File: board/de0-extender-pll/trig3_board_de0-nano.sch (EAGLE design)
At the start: 305 parts, among them IC1 ICL7660CPA, IC2 ICL7660CPA, IC3 ICL7660CPA, IC4 ICL7660CPA, J10 2p-2.54, J11 2p-2.54, J12 4p-2.54, J13 BU-SMB-V, J131 4p-2.54, J14 BU-SMB-V, J141 2p-2.54, J15 2p-2.54, J16 2p-2.54, J17 2p-2.54, J18 2p-2.54, J19 6HE-160-VG64AC, J20 4p-2.54, J21 4p-2.54, J22 2p-2.54, J23 2p-2.54, J24 2p-2.54, J25 2p-2.54, J26 4p-2.54, J27 4p-2.54, J28 2p-2.54, J29 2p-2.54, J3 4p-2.54, J30 2p-2.54, J31 2p-2.54, J311 4p-2.54, J32 2p-2.54, J33 2p-2.54, J34 2p-2.54, J35 2p-2.54, J36 2p-2.54, J37 2p-2.54, J38 2p-2.54, J39 2p-2.54, J4 2p-2.54, J40 2p-2.54, J41 2p-2.54, J42 2p-2.54, J43 2p-2.54, J48 2p-2.54, J49 2p-2.54, J5 2p-2.54, J50 2p-2.54, J51 2p-2.54, J52 2p-2.54, J53 2p-2.54, J54 2p-2.54, J55 2p-2.54, J6 2p-2.54, J7 4p-2.54, J8 2p-2.54, J9 2p-2.54, K15_R10P BU-SMB-V, K16_R10N BU-SMB-V, M16CLK_3N BU-SMB-V, P11 BU-SMB-V, P14_CLKOUT_4P BU-SMB-V, P15 BU-SMB-V, P16_R15N BU-SMB-V, P9 BU-SMB-V, T10_B16N BU-SMB-V, T12_B18N BU-SMB-V, T13_B20N BU-SMB-V, T14_B23P BU-SMB-V, T15_B23N BU-SMB-V, T9CLK_7N BU-SMB-V

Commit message: removed some unused inputs
kept all clock inputs and some extra inputs
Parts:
- removed A14_CLKOUT_2N, B7_T9P, C3_CLKOUT_3N, C9_T15N, D3_CLKOUT_3P, D9_T15P, G15_R5P, G16_R5N, N15_R13P, N16_R13N, P14_CLKOUT_4P, R10_B16P, R12_B18P, R14_CLKOUT_4N, T10_B16N, T12_B18N: BU-SMB-V, con-coax:BU-SMB-V
- removed J10, J11, J28, J29, J30, J31, J48, J49, J50, J51, J52, J53, J54, J55, J8, J9: 2p-2.54, Seeed-Connector:DIP-BLACK-MALE-HEADER-VERT(2P-2.54)
- removed R100, R111, R141, R24, R26, R27, R29, R45, R46, R47, R49, R50, R51, R52, R53, R91: 50, SparkFun-Passives:RESISTORAXIAL-0.3
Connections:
- net GND: no longer A14_CLKOUT_2N.2, B7_T9P.2, C3_CLKOUT_3N.2, C9_T15N.2, D3_CLKOUT_3P.2, D9_T15P.2, G15_R5P.2, G16_R5N.2, J10.1, J11.1, J28.1, J29.1, J30.1, J31.1, J48.1, J49.1, J50.1, J51.1, J52.1, J53.1, J54.1, J55.1, J8.1, J9.1, N15_R13P.2, N16_R13N.2, P14_CLKOUT_4P.2, R100.1, R10_B16P.2, R111.1, R12_B18P.2, R141.1, R14_CLKOUT_4N.2, R24.1, R26.1, R27.1, R29.1, R45.1, R46.1, R47.1, R49.1, R50.1, R51.1, R52.1, R53.1, R91.1, T10_B16N.2, T12_B18N.2
- net GPIO_00_D3: no longer D3_CLKOUT_3P.1, J50.2, R51.2
- net GPIO_012_B7: no longer B7_T9P.1, J49.2, R50.2
- net GPIO_01_C3: no longer C3_CLKOUT_3N.1, J30.2, R27.2
- net GPIO_024_C9: no longer C9_T15N.1, J8.2, R91.2
- net GPIO_025_D9: no longer D9_T15P.1, J11.2, R141.2
- net GPIO_111_R10: no longer J48.2, R10_B16P.1, R49.2
- net GPIO_122_R14: no longer J53.2, R14_CLKOUT_4N.1, R46.2
- net GPIO_123_N16: no longer J55.2, N16_R13N.1, R52.2
- net GPIO_124_N15: no longer J54.2, N15_R13P.1, R47.2
- net GPIO_125_P14: no longer J52.2, P14_CLKOUT_4P.1, R45.2
- net GPIO_15_T12: no longer J9.2, R100.2, T12_B18N.1
- net GPIO_16_R12: no longer J10.2, R111.2, R12_B18P.1
- net GPIO_18_T10: no longer J51.2, R53.2, T10_B16N.1
- net GPIO_20_A14: no longer A14_CLKOUT_2N.1, J31.2, R29.2
- net GPIO_211_G16: no longer G16_R5N.1, J28.2, R24.2
- net GPIO_212_G15: no longer G15_R5P.1, J29.2, R26.2
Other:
- note added: "pins used in design A6 B6 C11 E11 F9 K15 K16 L13 L14 N9 N11 P16 R9 R16 T9 R9/T9 N9 L13 L14 R16/P16 B6 A6 K15/K16 N11 F9 C11 E11 on board: clock R8, LEDs L3 B1 F3 D1 A11 B13 A13 A15 IN: K15, K16, P16 R16 R9 T9 OUT: A6, B6, C11, E11, N9, N11, F9 SERIAL: L13, L14"
- moved on the sheet: A12_T21N, A2_T2N, A3_T2P, A8CLK_4N, B12_T21P, B8CLK_4P, E15CLK_2P, E16CLK_2N, F8_T10P, K15_R10P, M16CLK_3N, R11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

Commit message: removed many outputs and negative voltage
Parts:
- removed A4, A5, B11, B16, B3, B4, B5, C14, C15, C6, C8, D11, D12, D14, D15, D16, D5, D6, D8, E10, E6, E9, F14, F15, F16, J14, N12, N14: BU-SMB-V, con-coax:BU-SMB-V
- removed C10, C5, C91, C93, C94, C95, C97: 0.1uF, SparkFun-Capacitors:CAP0805
- removed OJ1, OJ17, OJ18, OJ19, OJ2, OJ20, OJ21, OJ22, OJ23, OJ24, OJ25, OJ26, OJ27, OJ28, OJ29, OJ3, OJ30, OJ31, OJ32, OJ33, OJ34, OJ35, OJ36, OJ37, OJ38, OJ39, OJ4, OJ40, OJ49, OJ5, OJ50, OJ51, OJ52, OJ53, OJ54, OJ55, OJ56, OJ6, OJ65, OJ66, OJ67, OJ68, OJ69, OJ7, OJ70, OJ71, OJ72, OJ8, OJ89, OJ90, OJ91, OJ92, OJ93, OJ94, OJ95, OJ96: 2p-2.54, Seeed-Connector:DIP-BLACK-MALE-HEADER-VERT(2P-2.54)
- removed VSLUE, VSLUE11, VSLUE2, VSLUE3, VSLUE4, VSLUE6, VSLUE8: SN74ACT244DW, SN74ACT244DW:SN74ACT244DW
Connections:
- removed net OUT1: J14.1, OJ1.1, VSLUE.1Y1, VSLUE.1Y2
- removed net OUT10: E9.1, OJ19.1, VSLUE2.1Y3, VSLUE2.1Y4
- removed net OUT11: D8.1, OJ17.1, VSLUE2.2Y3, VSLUE2.2Y4
- removed net OUT12: B16.1, OJ18.1, VSLUE2.2Y1, VSLUE2.2Y2
- removed net OUT13: C15.1, OJ28.1, VSLUE3.1Y1, VSLUE3.1Y2
- removed net OUT14: C14.1, OJ27.1, VSLUE3.1Y3, VSLUE3.1Y4
- removed net OUT15: D15.1, OJ25.1, VSLUE3.2Y3, VSLUE3.2Y4
- removed net OUT16: F14.1, OJ26.1, VSLUE3.2Y1, VSLUE3.2Y2
- removed net OUT17: D16.1, OJ36.1, VSLUE4.1Y1, VSLUE4.1Y2
- removed net OUT18: D14.1, OJ35.1, VSLUE4.1Y3, VSLUE4.1Y4
- removed net OUT19: F15.1, OJ33.1, VSLUE4.2Y3, VSLUE4.2Y4
- removed net OUT2: D11.1, OJ2.1, VSLUE.1Y3, VSLUE.1Y4
- removed net OUT20: F16.1, OJ34.1, VSLUE4.2Y1, VSLUE4.2Y2
- removed net OUT25: D6.1, OJ52.1, VSLUE6.1Y1, VSLUE6.1Y2
- removed net OUT26: C6.1, OJ51.1, VSLUE6.1Y3, VSLUE6.1Y4
- removed net OUT27: C8.1, OJ49.1, VSLUE6.2Y3, VSLUE6.2Y4
- removed net OUT28: E6.1, OJ50.1, VSLUE6.2Y1, VSLUE6.2Y2
- removed net OUT3: B11.1, OJ3.1, VSLUE.2Y1, VSLUE.2Y2
- removed net OUT33: B5.1, OJ68.1, VSLUE8.1Y1, VSLUE8.1Y2
- removed net OUT34: A5.1, OJ67.1, VSLUE8.1Y3, VSLUE8.1Y4
- removed net OUT35: D5.1, OJ65.1, VSLUE8.2Y3, VSLUE8.2Y4
- removed net OUT36: N14.1, OJ66.1, VSLUE8.2Y1, VSLUE8.2Y2
- removed net OUT4: E10.1, OJ4.1, VSLUE.2Y3, VSLUE.2Y4
- removed net OUT45: D12.1, OJ92.1, VSLUE11.1Y1, VSLUE11.1Y2
- removed net OUT46: B3.1, OJ91.1, VSLUE11.1Y3, VSLUE11.1Y4
- removed net OUT47: A4.1, OJ89.1, VSLUE11.2Y3, VSLUE11.2Y4
- removed net OUT48: B4.1, OJ90.1, VSLUE11.2Y1, VSLUE11.2Y2
- removed net OUT9: N12.1, OJ20.1, VSLUE2.1Y1, VSLUE2.1Y2
- net 5V: no longer C10.2, C5.2, C91.2, C93.2, C94.2, C95.2, C97.2, VSLUE.VCC, VSLUE11.VCC, VSLUE2.VCC, VSLUE3.VCC, VSLUE4.VCC, VSLUE6.VCC, VSLUE8.VCC
- net GND: no longer A4.2, A5.2, B11.2, B16.2, B3.2, B4.2, B5.2, C10.1, C14.2, C15.2, C5.1, C6.2, C8.2, C91.1, C93.1, C94.1, C95.1, C97.1, D11.2, D12.2, D14.2, D15.2, D16.2, D5.2, D6.2, D8.2, E10.2, E6.2, E9.2, F14.2, F15.2, F16.2, J14.2, N12.2, N14.2, OJ1.2, OJ17.2, OJ18.2, OJ19.2, OJ2.2, OJ20.2, OJ21.2, OJ22.2, OJ23.2, OJ24.2, OJ25.2, OJ26.2, OJ27.2, OJ28.2, OJ29.2, OJ3.2, OJ30.2, OJ31.2, OJ32.2, OJ33.2, OJ34.2, OJ35.2, OJ36.2, OJ37.2, OJ38.2, OJ39.2, OJ4.2, OJ40.2, OJ49.2, OJ5.2, OJ50.2, OJ51.2, OJ52.2, OJ53.2, OJ54.2, OJ55.2, OJ56.2, OJ6.2, OJ65.2, OJ66.2, OJ67.2, OJ68.2, OJ69.2, OJ7.2, OJ70.2, OJ71.2, OJ72.2, OJ8.2, OJ89.2, OJ90.2, OJ91.2, OJ92.2, OJ93.2, OJ94.2, OJ95.2, OJ96.2, VSLUE.GND, VSLUE11.GND, VSLUE2.GND, VSLUE3.GND, VSLUE4.GND, VSLUE6.GND, VSLUE8.GND
- net GPIO_013_D6: no longer OJ55.1, VSLUE6.1A1, VSLUE6.1A2
- net GPIO_015_C6: no longer OJ56.1, VSLUE6.1A3, VSLUE6.1A4
- net GPIO_016_C8: no longer OJ53.1, VSLUE6.2A3, VSLUE6.2A4
- net GPIO_017_E6: no longer OJ54.1, VSLUE6.2A1, VSLUE6.2A2
- net GPIO_019_D8: no longer OJ21.1, VSLUE2.2A3, VSLUE2.2A4
- net GPIO_023_E9: no longer OJ24.1, VSLUE2.1A3, VSLUE2.1A4
- net GPIO_027_E10: no longer OJ5.1, VSLUE.2A3, VSLUE.2A4
- net GPIO_029_B11: no longer OJ6.1, VSLUE.2A1, VSLUE.2A2
- net GPIO_031_D11: no longer OJ8.1, VSLUE.1A3, VSLUE.1A4
- net GPIO_032_D12: no longer OJ95.1, VSLUE11.1A1, VSLUE11.1A2
- net GPIO_04_B3: no longer OJ96.1, VSLUE11.1A3, VSLUE11.1A4
- net GPIO_05_B4: no longer OJ94.1, VSLUE11.2A1, VSLUE11.2A2
- net GPIO_06_A4: no longer OJ93.1, VSLUE11.2A3, VSLUE11.2A4
- net GPIO_07_B5: no longer OJ71.1, VSLUE8.1A1, VSLUE8.1A2
- net GPIO_08_A5: no longer OJ72.1, VSLUE8.1A3, VSLUE8.1A4
- net GPIO_09_D5: no longer OJ69.1, VSLUE8.2A3, VSLUE8.2A4
- net GPIO_112_N12: no longer OJ23.1, VSLUE2.1A1, VSLUE2.1A2
- net GPIO_114_N9: no longer VSLUE.!1OE, VSLUE.!2OE, VSLUE11.!1OE, VSLUE11.!2OE, VSLUE2.!1OE, VSLUE2.!2OE, VSLUE3.!1OE, VSLUE3.!2OE, VSLUE4.!1OE, VSLUE4.!2OE, VSLUE6.!1OE, VSLUE6.!2OE, VSLUE8.!1OE, VSLUE8.!2OE
- net GPIO_127_N14: no longer OJ70.1, VSLUE8.2A1, VSLUE8.2A2
- net GPIO_133_J14: no longer OJ7.1, VSLUE.1A1, VSLUE.1A2
- net GPIO_210_F14: no longer OJ30.1, VSLUE3.2A1, VSLUE3.2A2
- net GPIO_21_B16: no longer OJ22.1, VSLUE2.2A1, VSLUE2.2A2
- net GPIO_22_C14: no longer OJ32.1, VSLUE3.1A3, VSLUE3.1A4
- net GPIO_24_C15: no longer OJ31.1, VSLUE3.1A1, VSLUE3.1A2
- net GPIO_25_D16: no longer OJ39.1, VSLUE4.1A1, VSLUE4.1A2
- net GPIO_26_D15: no longer OJ29.1, VSLUE3.2A3, VSLUE3.2A4
- net GPIO_27_D14: no longer OJ40.1, VSLUE4.1A3, VSLUE4.1A4
- net GPIO_28_F15: no longer OJ37.1, VSLUE4.2A3, VSLUE4.2A4
- net GPIO_29_F16: no longer OJ38.1, VSLUE4.2A1, VSLUE4.2A2

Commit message: more removal
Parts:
- removed C1, C12, C13, C17, C18, C3, C7, C9: 10uF, SparkFun-Capacitors:CAPPTH1
- removed C19, C20, C21, C22: 0.1uF, SparkFun-Capacitors:CAP0805
- removed IC1, IC2, IC3, IC4: ICL7660CPA, maxim:ICL7660CPA
- removed J1: (no value), SparkFun-Connectors:M13X22X13
- removed J131, J311: 4p-2.54, Seeed-Connector:DIP-BLACK-FEMALE-HEADER-VERT(4P-2.54)
- removed J19: 6HE-160-VG64AC, 19inch:6HE-160-VG64AC
- removed J20, J21, J26, J27: 4p-2.54, Seeed-Connector:DIP-BLACK-MALE-HEADER-VERT(4P-2.54)
- removed OJ10, OJ11, OJ12, OJ9: 2p-2.54, Seeed-Connector:DIP-BLACK-MALE-HEADER-VERT(2P-2.54)
- removed R1, R2, R3, R7: 3296W 5k, resistor:R-TRIMM3296W
- removed R10, R12, R13, R14: 1k, SparkFun-Passives:RESISTORAXIAL-0.3
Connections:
- removed net -3V3_1: C3.1, IC1.VOUT, J20.P$1, R10.2
- removed net -3V3_2: C9.1, IC2.VOUT, J21.P$1, R12.2
- removed net -3V3_3: C13.1, IC3.VOUT, J26.P$1, R13.2
- removed net -3V3_4: C18.1, IC4.VOUT, J27.P$1, R14.2
- removed net -V1: C19.2, J20.P$2, OJ9.1, R1.S
- removed net -V2: C20.2, J21.P$2, OJ10.1, R2.S
- removed net -V3: C21.2, J26.P$2, OJ11.1, R3.S
- removed net -V4: C22.2, J27.P$2, OJ12.1, R7.S
- removed net AIN0: J1.24, J131.P$4
- removed net AIN1: J1.25, J311.P$1
- removed net AIN2: J1.22, J131.P$3
- removed net AIN3: J1.21, J311.P$3
- removed net AIN4: J1.23, J311.P$2
- removed net AIN5: J1.18, J131.P$1
- removed net AIN6: J1.19, J311.P$4
- removed net AIN7: J1.20, J131.P$2
- removed net GPIO_20_A14: J1.5
- removed net GPIO_210_F14: J1.15
- removed net GPIO_211_G16: J1.16
- removed net GPIO_212_G15: J1.17
- removed net GPIO_21_B16: J1.6
- removed net GPIO_22_C14: J1.7
- removed net GPIO_24_C15: J1.9
- removed net GPIO_25_D16: J1.10
- removed net GPIO_26_D15: J1.11
- removed net GPIO_27_D14: J1.12
- removed net GPIO_28_F15: J1.13
- removed net GPIO_29_F16: J1.14
- removed net N$1: C1.1, IC1.CAP+
- removed net N$10: R1.E, R10.1
- removed net N$11: R12.1, R2.E
- removed net N$12: R13.1, R3.E
- removed net N$13: R14.1, R7.E
- removed net N$2: C1.2, IC1.CAP-
- removed net N$3: C12.1, IC3.CAP+
- removed net N$4: C7.1, IC2.CAP+
- removed net N$5: C7.2, IC2.CAP-
- removed net N$6: C12.2, IC3.CAP-
- removed net N$7: C17.1, IC4.CAP+
- removed net N$8: C17.2, IC4.CAP-
- net 3V3: no longer IC1.V+, IC2.V+, IC3.V+, IC4.V+, J1.1, J20.P$4, J21.P$4, J26.P$4, J27.P$4
- net 5V: no longer J191-A32.MS, J191-C32.MS, J192-A32.MS, J192-C32.MS
- net GND: no longer C13.2, C18.2, C19.1, C20.1, C21.1, C22.1, C3.2, C9.2, IC1.GND, IC2.GND, IC3.GND, IC4.GND, J1.26, J191-A9.MS, J191-C9.MS, J192-A9.MS, J192-C9.MS, J20.P$3, J21.P$3, J26.P$3, J27.P$3, R1.A, R2.A, R3.A, R7.A
- net GPIO_014_A7: no longer OJ9.2
- net GPIO_020_E8: no longer OJ12.2
- net GPIO_030_A12: no longer OJ10.2
- net GPIO_11_T15: no longer OJ11.2
- net GPIO_23_C16: no longer J1.8
- net GPIO_2_IN0_E15CLK: no longer J1.2
- net GPIO_2_IN1_E16CLK: no longer J1.3
- net GPIO_2_IN2_M16CLK: no longer J1.4

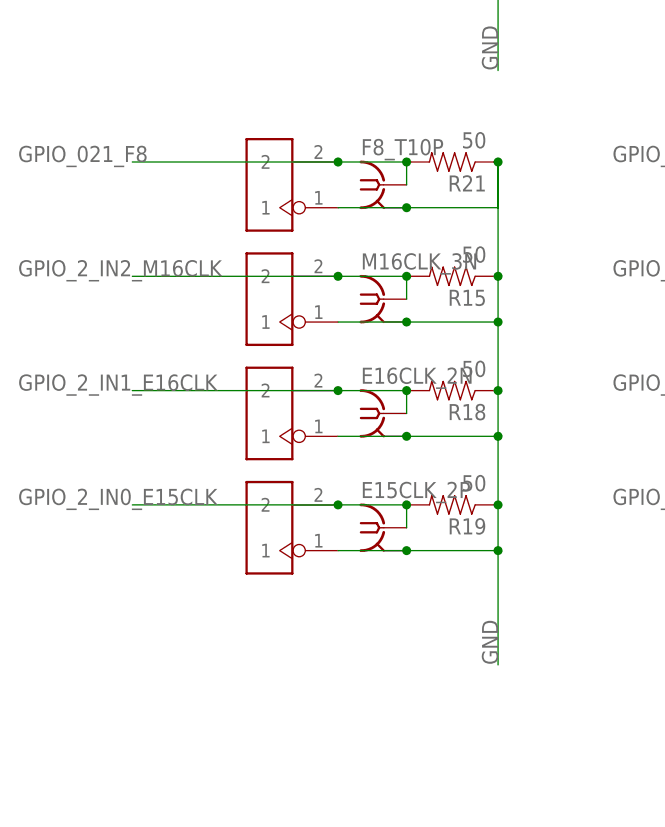
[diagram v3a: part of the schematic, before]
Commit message: going to delete more ins/outs
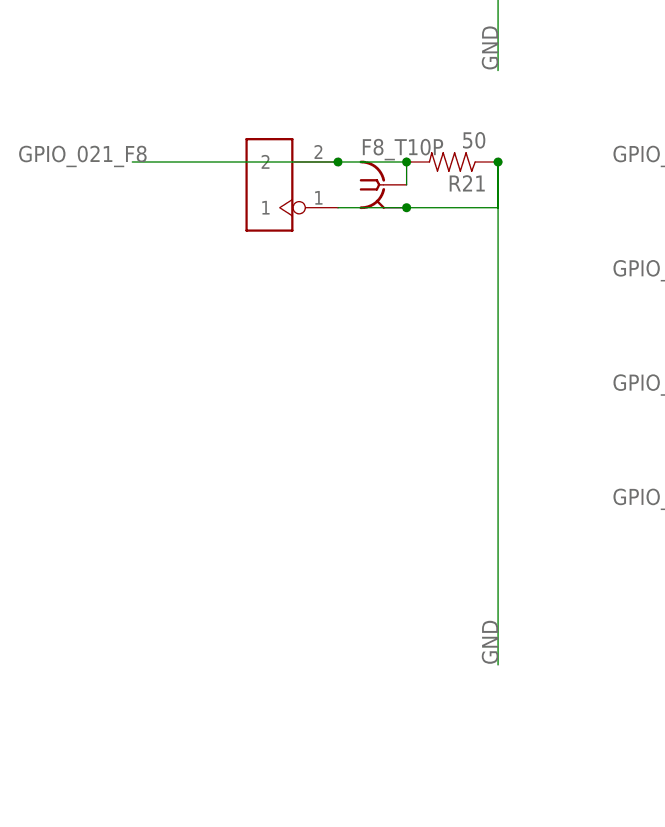
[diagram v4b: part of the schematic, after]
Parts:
- removed E15CLK_2P, E16CLK_2N, M16CLK_3N: BU-SMB-V, con-coax:BU-SMB-V
- removed J141, J15, J16: 2p-2.54, Seeed-Connector:DIP-BLACK-MALE-HEADER-VERT(2P-2.54)
- removed R15, R18, R19: 50, SparkFun-Passives:RESISTORAXIAL-0.3
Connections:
- removed net GPIO_2_IN0_E15CLK: E15CLK_2P.1, J16.2, R19.2
- removed net GPIO_2_IN1_E16CLK: E16CLK_2N.1, J15.2, R18.2
- removed net GPIO_2_IN2_M16CLK: J141.2, M16CLK_3N.1, R15.2
- net GND: no longer E15CLK_2P.2, E16CLK_2N.2, J141.1, J15.1, J16.1, M16CLK_3N.2, R15.1, R18.1, R19.1
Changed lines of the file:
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@@
 <part name="SV2" library="con-lsta" deviceset="FE20-2" device=""/>
 <part name="J2" library="SparkFun-Connectors" deviceset="M13X2" device="2X13"/>
-<part name="M16CLK_3N" library="con-coax" library_urn="urn:adsk.eagle:library:133" deviceset="BU-SMB-V" device="" package3d_urn="urn:adsk.eagle:package:6209/1"/>
-<part name="E16CLK_2N" library="con-coax" library_urn="urn:adsk.eagle:library:133" deviceset="BU-SMB-V" device="" package3d_urn="urn:adsk.eagle:package:6209/1"/>
-<part name="E15CLK_2P" library="con-coax" library_urn="urn:adsk.eagle:library:133" deviceset="BU-SMB-V" device="" package3d_urn="urn:adsk.eagle:package:6209/1"/>
-<part name="J141" library="Seeed-Connector" library_urn="urn:adsk.eagle:library:478" deviceset="DIP-BLACK-MALE-HEADER-VERT(2P-2.54)" device="" package3d_urn="urn:adsk.eagle:package:33132/1" value="2p-2.54"/>
-<part name="J15" library="Seeed-Connector" library_urn="urn:adsk.eagle:library:478" deviceset="DIP-BLACK-MALE-HEADER-VERT(2P-2.54)" device="" package3d_urn="urn:adsk.eagle:package:33132/1" value="2p-2.54"/>
-<part name="J16" library="Seeed-Connector" library_urn="urn:adsk.eagle:library:478" deviceset="DIP-BLACK-MALE-HEADER-VERT(2P-2.54)" device="" package3d_urn="urn:adsk.eagle:package:33132/1" value="2p-2.54"/>
-<part name="R15" library="SparkFun-Passives" deviceset="RESISTOR" device="AXIAL-0.3" value="50"/>
-<part name="R18" library="SparkFun-Passives" deviceset="RESISTOR" device="AXIAL-0.3" value="50"/>
-<part name="R19" library="SparkFun-Passives" deviceset="RESISTOR" device="AXIAL-0.3" value="50"/>
 <part name="F8_T10P" library="con-coax" library_urn="urn:adsk.eagle:library:133" deviceset="BU-SMB-V" device="" package3d_urn="urn:adsk.eagle:package:6209/1"/>
 <part name="J18" library="Seeed-Connector" library_urn="urn:adsk.eagle:library:478" deviceset="DIP-BLACK-MALE-HEADER-VERT(2P-2.54)" device="" package3d_urn="urn:adsk.eagle:package:33132/1" value="2p-2.54"/>
@@
 <attribute name="NAME" x="107.442" y="33.02" size="1.778" layer="95" rot="R270"/>
 </instance>
-<instance part="M16CLK_3N" gate="G1" x="-66.04" y="101.6" smashed="yes">
-<attribute name="NAME" x="-68.58" y="104.902" size="1.778" layer="95"/>
-</instance>
-<instance part="E16CLK_2N" gate="G1" x="-66.04" y="88.9" smashed="yes">
-<attribute name="NAME" x="-68.58" y="92.202" size="1.778" layer="95"/>
-</instance>
-<instance part="E15CLK_2P" gate="G1" x="-66.04" y="76.2" smashed="yes">
-<attribute name="NAME" x="-68.58" y="79.502" size="1.778" layer="95"/>
-</instance>
-<instance part="J141" gate="G$1" x="-78.74" y="101.6" smashed="yes" rot="R180"/>
-<instance part="J15" gate="G$1" x="-78.74" y="88.9" smashed="yes" rot="R180"/>
-<instance part="J16" gate="G$1" x="-78.74" y="76.2" smashed="yes" rot="R180"/>
-<instance part="R15" gate="G$1" x="-58.42" y="104.14" smashed="yes" rot="R180">
-<attribute name="NAME" x="-54.61" y="102.6414" size="1.778" layer="95" rot="R180"/>
-<attribute name="VALUE" x="-54.61" y="107.442" size="1.778" layer="96" rot="R180"/>
-</instance>
-<instance part="R18" gate="G$1" x="-58.42" y="91.44" smashed="yes" rot="R180">
-<attribute name="NAME" x="-54.61" y="89.9414" size="1.778" layer="95" rot="R180"/>
-<attribute name="VALUE" x="-54.61" y="94.742" size="1.778" layer="96" rot="R180"/>
-</instance>
-<instance part="R19" gate="G$1" x="-58.42" y="78.74" smashed="yes" rot="R180">
-<attribute name="NAME" x="-54.61" y="77.2414" size="1.778" layer="95" rot="R180"/>
-<attribute name="VALUE" x="-54.61" y="82.042" size="1.778" layer="96" rot="R180"/>
-</instance>
 <instance part="F8_T10P" gate="G1" x="-66.04" y="114.3" smashed="yes">
 <attribute name="NAME" x="-68.58" y="117.602" size="1.778" layer="95"/>
@@
 <junction x="-63.5" y="111.76"/>
 <wire x1="-53.34" y1="111.76" x2="-63.5" y2="111.76" width="0.1524" layer="91"/>
-<pinref part="J141" gate="G$1" pin="1"/>
-<pinref part="M16CLK_3N" gate="G1" pin="2"/>
-<wire x1="-63.5" y1="99.06" x2="-71.12" y2="99.06" width="0.1524" layer="91"/>
-<junction x="-63.5" y="99.06"/>
-<wire x1="-63.5" y1="99.06" x2="-53.34" y2="99.06" width="0.1524" layer="91"/>
-<junction x="-53.34" y="99.06"/>
-<pinref part="E16CLK_2N" gate="G1" pin="2"/>
-<pinref part="J15" gate="G$1" pin="1"/>
-<wire x1="-71.12" y1="86.36" x2="-63.5" y2="86.36" width="0.1524" layer="91"/>
-<junction x="-63.5" y="86.36"/>
-<wire x1="-63.5" y1="86.36" x2="-53.34" y2="86.36" width="0.1524" layer="91"/>
-<junction x="-53.34" y="86.36"/>
-<pinref part="J16" gate="G$1" pin="1"/>
-<pinref part="E15CLK_2P" gate="G1" pin="2"/>
-<wire x1="-63.5" y1="73.66" x2="-71.12" y2="73.66" width="0.1524" layer="91"/>
-<junction x="-63.5" y="73.66"/>
-<wire x1="-63.5" y1="73.66" x2="-53.34" y2="73.66" width="0.1524" layer="91"/>
-<wire x1="-53.34" y1="73.66" x2="-53.34" y2="60.96" width="0.1524" layer="91"/>
-<junction x="-53.34" y="73.66"/>
-<wire x1="-53.34" y1="73.66" x2="-53.34" y2="78.74" width="0.1524" layer="91"/>
-<pinref part="R19" gate="G$1" pin="1"/>
-<junction x="-53.34" y="78.74"/>
-<wire x1="-53.34" y1="78.74" x2="-53.34" y2="86.36" width="0.1524" layer="91"/>
-<wire x1="-53.34" y1="86.36" x2="-53.34" y2="91.44" width="0.1524" layer="91"/>
-<pinref part="R18" gate="G$1" pin="1"/>
-<junction x="-53.34" y="91.44"/>
-<wire x1="-53.34" y1="91.44" x2="-53.34" y2="99.06" width="0.1524" layer="91"/>
-<wire x1="-53.34" y1="99.06" x2="-53.34" y2="104.14" width="0.1524" layer="91"/>
-<pinref part="R15" gate="G$1" pin="1"/>
-<junction x="-53.34" y="104.14"/>
-<wire x1="-53.34" y1="104.14" x2="-53.34" y2="116.84" width="0.1524" layer="91"/>
+<wire x1="-53.34" y1="60.96" x2="-53.34" y2="116.84" width="0.1524" layer="91"/>
 <pinref part="R21" gate="G$1" pin="1"/>
 <junction x="-53.34" y="116.84"/>
@@
 </segment>
 </net>
-<net name="GPIO_2_IN1_E16CLK" class="0">
-<segment>
-<pinref part="E16CLK_2N" gate="G1" pin="1"/>
-<pinref part="J15" gate="G$1" pin="2"/>
-<wire x1="-63.5" y1="88.9" x2="-63.5" y2="91.44" width="0.1524" layer="91"/>
-<wire x1="-63.5" y1="91.44" x2="-71.12" y2="91.44" width="0.1524" layer="91"/>
-<pinref part="R18" gate="G$1" pin="2"/>
-<junction x="-63.5" y="91.44"/>
-<wire x1="-71.12" y1="91.44" x2="-93.98" y2="91.44" width="0.1524" layer="91"/>
-<junction x="-71.12" y="91.44"/>
-<label x="-106.68" y="91.44" size="1.778" layer="95"/>
-</segment>
-</net>
-<net name="GPIO_2_IN0_E15CLK" class="0">
-<segment>
-<pinref part="J16" gate="G$1" pin="2"/>
-<pinref part="E15CLK_2P" gate="G1" pin="1"/>
-<wire x1="-63.5" y1="76.2" x2="-63.5" y2="78.74" width="0.1524" layer="91"/>
-<wire x1="-63.5" y1="78.74" x2="-71.12" y2="78.74" width="0.1524" layer="91"/>
-<pinref part="R19" gate="G$1" pin="2"/>
-<junction x="-63.5" y="78.74"/>
-<wire x1="-71.12" y1="78.74" x2="-93.98" y2="78.74" width="0.1524" layer="91"/>
-<junction x="-71.12" y="78.74"/>
-<label x="-106.68" y="78.74" size="1.778" layer="95"/>
-</segment>
-</net>
-<net name="GPIO_2_IN2_M16CLK" class="0">
-<segment>
-<pinref part="M16CLK_3N" gate="G1" pin="1"/>
-<pinref part="J141" gate="G$1" pin="2"/>
-<wire x1="-63.5" y1="101.6" x2="-63.5" y2="104.14" width="0.1524" layer="91"/>
-<wire x1="-63.5" y1="104.14" x2="-71.12" y2="104.14" width="0.1524" layer="91"/>
-<pinref part="R15" gate="G$1" pin="2"/>
-<junction x="-63.5" y="104.14"/>
-<wire x1="-71.12" y1="104.14" x2="-93.98" y2="104.14" width="0.1524" layer="91"/>
-<junction x="-71.12" y="104.14"/>
-<label x="-106.68" y="104.14" size="1.778" layer="95"/>
-</segment>
-</net>
